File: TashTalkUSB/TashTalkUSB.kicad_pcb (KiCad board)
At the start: 2 copper layers, 60 x 25 mm, 35 parts, among them J1 TC2030, J3 USB_C_Receptacle_USB2.0_14P, U1 CP2102N-Axx-xQFN20, U2 PIC12F1840-xSN, U3 SN65HVD1473DGSR

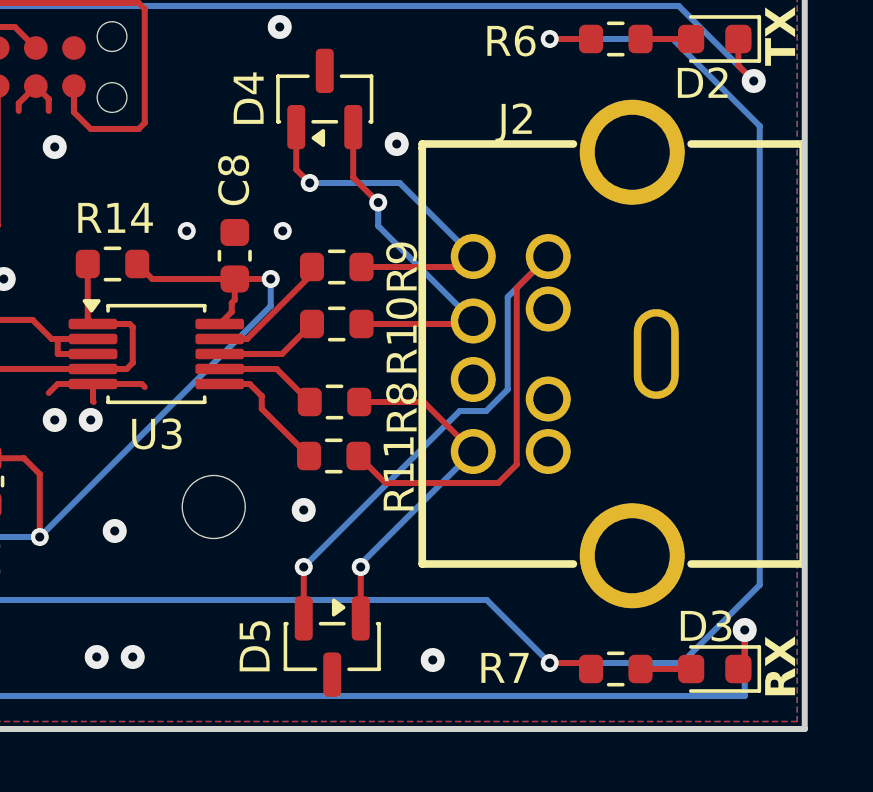
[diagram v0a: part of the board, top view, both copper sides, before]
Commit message: Update PCB and schematic with fixed mini-DIN 8 pinout
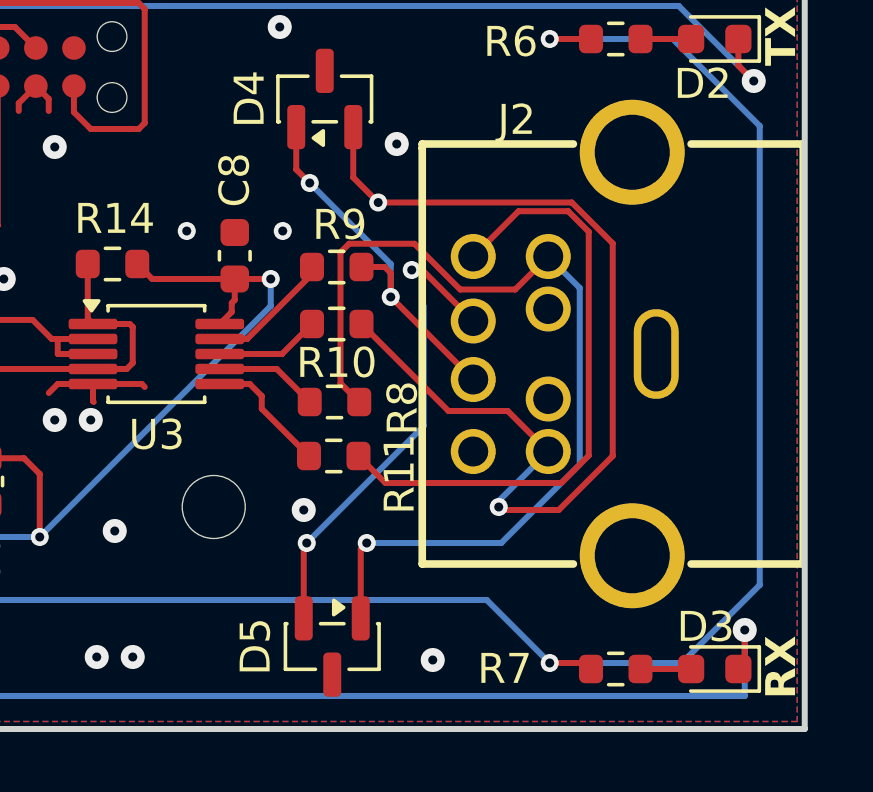
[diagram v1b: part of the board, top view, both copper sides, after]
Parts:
- R6: value R_Small -> 300
- R7: value R_Small -> 240
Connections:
- D5 pad 1: Z -> DIN3
- D5 pad 2: Y -> DIN6
- J2 pad 1: unconnected-(J2-Pad1) -> DIN1
- J2 pad 2: unconnected-(J2-Pad2) -> DIN2
- J2 pad 3: Y -> DIN3
- J2 pad 4: GND -> B
- J2 pad 5: A -> DIN6
- J2 pad 6: Z -> DIN7
- J2 pad 7: unconnected-(J2-Pad7) -> A
- J2 pad 8: B -> GND
- R11 pad 2: Y -> DIN6
- R8 pad 2: Z -> DIN3
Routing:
- net DIN6: track 0.00 -> 32.9 mm, vias 0 -> 1
- net DIN3: track 0.00 -> 31.5 mm, vias 0 -> 1
- net Y: track 29.2 -> 0.00 mm, vias 1 -> 0
- net B: track 11.9 -> 33.4 mm, vias 1 -> 2
- net Z: track 11.6 -> 0.00 mm, vias 1 -> 0
- net GND: track 12.7 -> 15.7 mm, vias 31 -> 32
- net A: track 12.4 -> 12.7 mm, vias 1 -> 2

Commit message: TashTalk USB Rev 2
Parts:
- D1: moved to F.Cu
- moved D1 7.93 mm to (167.4, 105.1)
- moved D5 0.25 mm to (204.3, 122.0)
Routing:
- net D+: track 14.9 -> 25.9 mm, vias 2 -> 3
- net DIN3: track 31.5 -> 22.1 mm, vias 1 -> 2
- net D-: track 18.7 -> 26.9 mm, vias 2 -> 3
- net DIN6: track 32.9 -> 27.0 mm, vias 1 -> 2
- net +5V: track 100.5 -> 100.7 mm, vias 4 -> 3
- net GND: vias 32 -> 34
- net B: vias 2 -> 1
